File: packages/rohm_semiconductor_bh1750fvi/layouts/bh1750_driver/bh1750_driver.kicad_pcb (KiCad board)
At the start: 2 copper layers, 4 parts

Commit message: WIP update packages till ESPs
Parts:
- C1, C2: footprint atopile:C0402-b3ef17 -> Samsung_Electro_Mechanics_CL05B104KO5NNNC:C0402
- R1: footprint atopile:R0402-56259e -> UNI_ROYAL_0402WGF1001TCE:R0402
- U1: footprint atopile:WSOF-6_L2.6-W1.6-P0.50-TL-EP-b2dfd8 -> ROHM_Semicon_BH1750FVI_TR:WSOF-6_L2.6-W1.6-P0.50-TL-EP

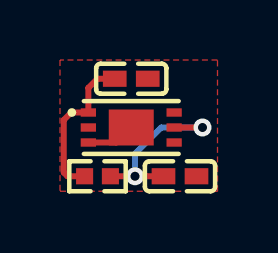
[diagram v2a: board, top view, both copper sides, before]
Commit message: Update 3D model locations
fix missing renders
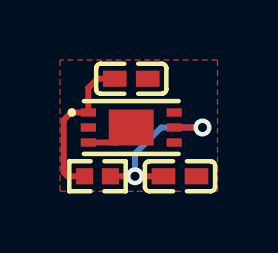
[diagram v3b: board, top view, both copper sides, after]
